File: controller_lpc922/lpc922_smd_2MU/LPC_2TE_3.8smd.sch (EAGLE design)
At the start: 46 parts, among them IC1 MC34063AD, Q1 BC856, Q2 BC847C, Q3 BCP52

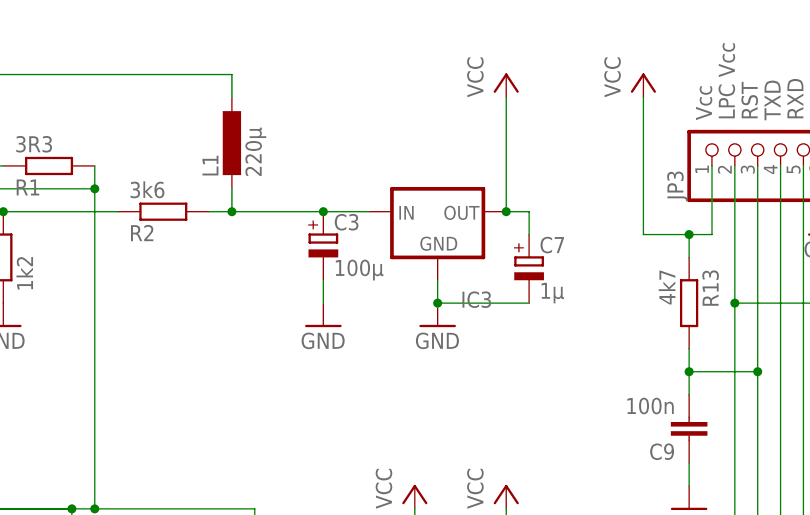
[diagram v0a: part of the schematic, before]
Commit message: Type of LDO added (VALUE in Schematic and Board added).
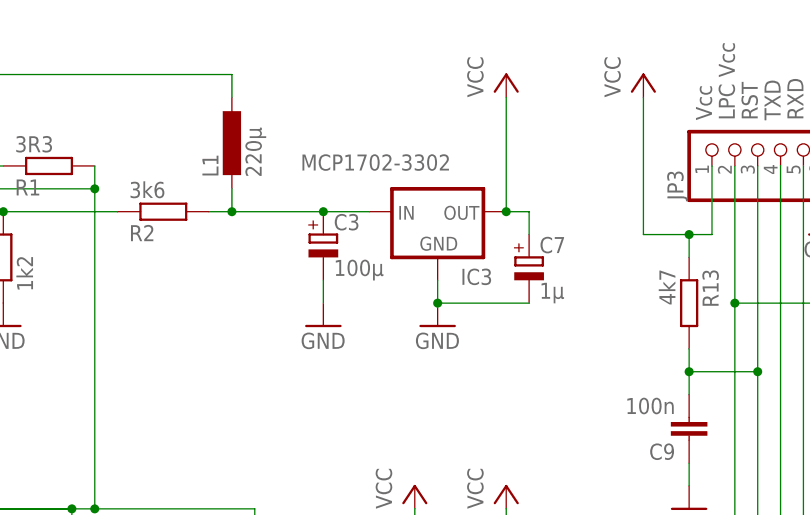
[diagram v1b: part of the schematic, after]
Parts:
- IC3: value (none) -> MCP1702-3302
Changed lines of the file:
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@@
 <part name="Q4" library="crystal" deviceset="ASF*" device="" technology="L1"/>
 <part name="GND3" library="supply1" deviceset="GND" device=""/>
-<part name="IC3" library="v-reg" deviceset="79LXX" device=""/>
+<part name="IC3" library="v-reg" deviceset="79LXX" device="" value="MCP1702-3302"/>
 <part name="C7" library="rcl" deviceset="CPOL-EU" device="E2-5" value="1µ"/>
 <part name="Q2" library="transistor-npn" deviceset="BC847*" device="SMD" technology="C" value="BC847C"/>
@@
 </instance>
 <instance part="IC3" gate="A" x="134.62" y="152.4" smashed="yes" rot="MR180">
-<attribute name="NAME" x="137.16" y="143.51" size="1.778" layer="95" rot="MR180"/>
-<attribute name="VALUE" x="137.16" y="146.05" size="1.778" layer="96" rot="MR180"/>
+<attribute name="NAME" x="137.16" y="146.05" size="1.778" layer="95" rot="MR180"/>
+<attribute name="VALUE" x="119.38" y="158.75" size="1.778" layer="96" rot="MR180"/>
 </instance>
 <instance part="C7" gate="G$1" x="144.78" y="147.32" smashed="yes">

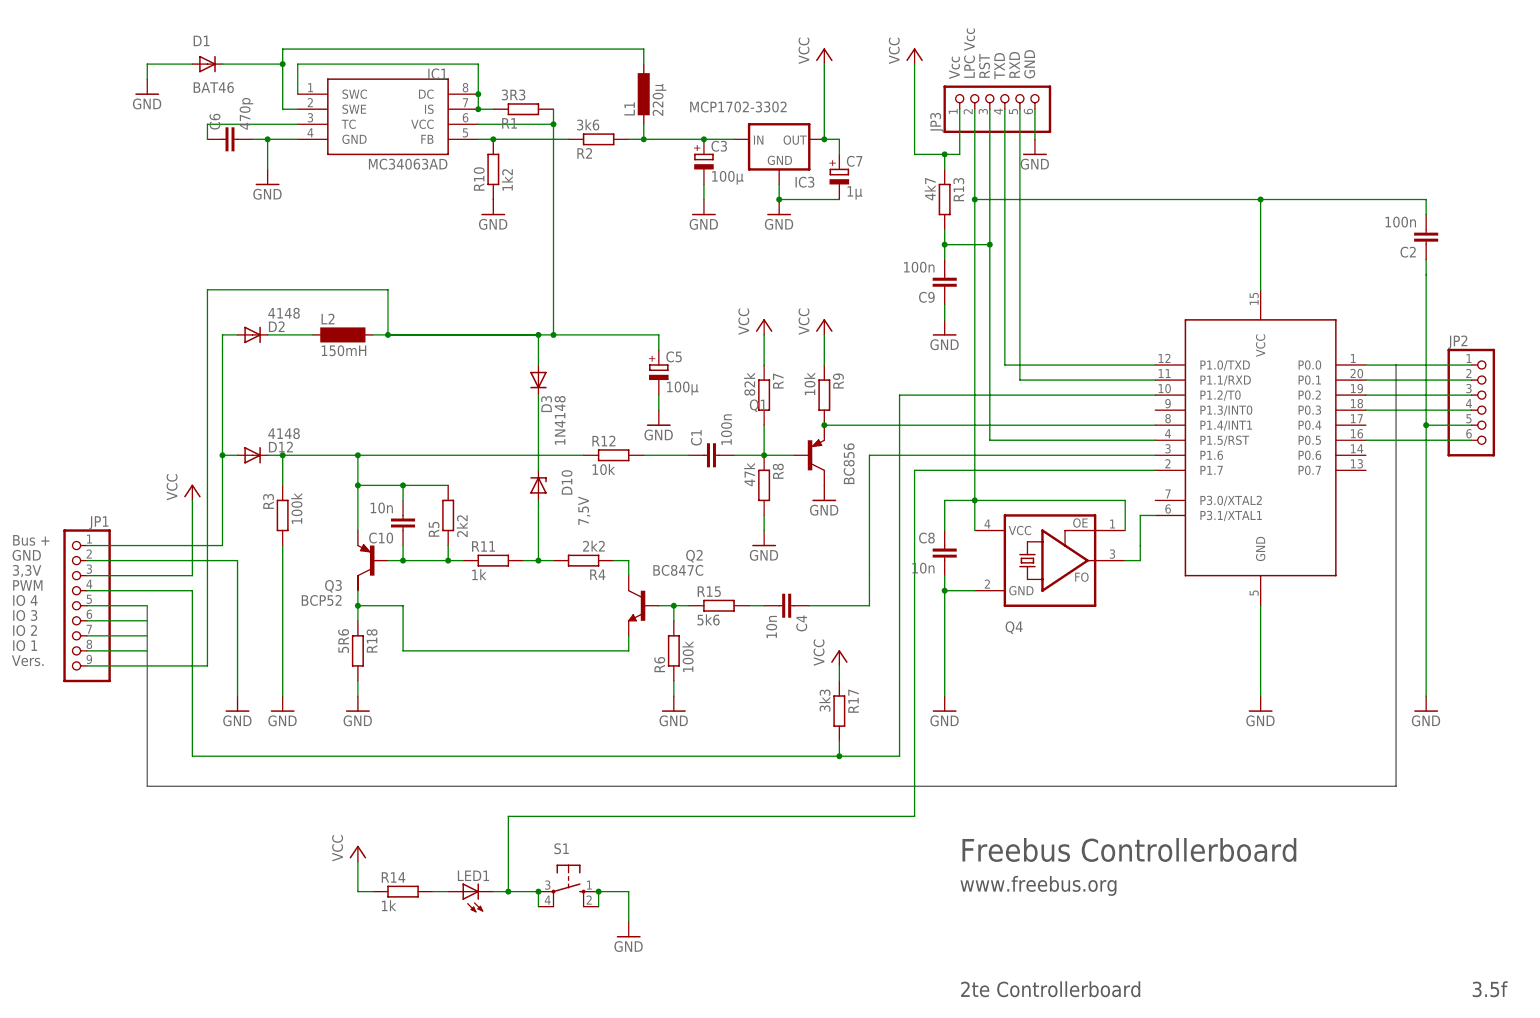
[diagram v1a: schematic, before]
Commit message: 3D models added + some rework
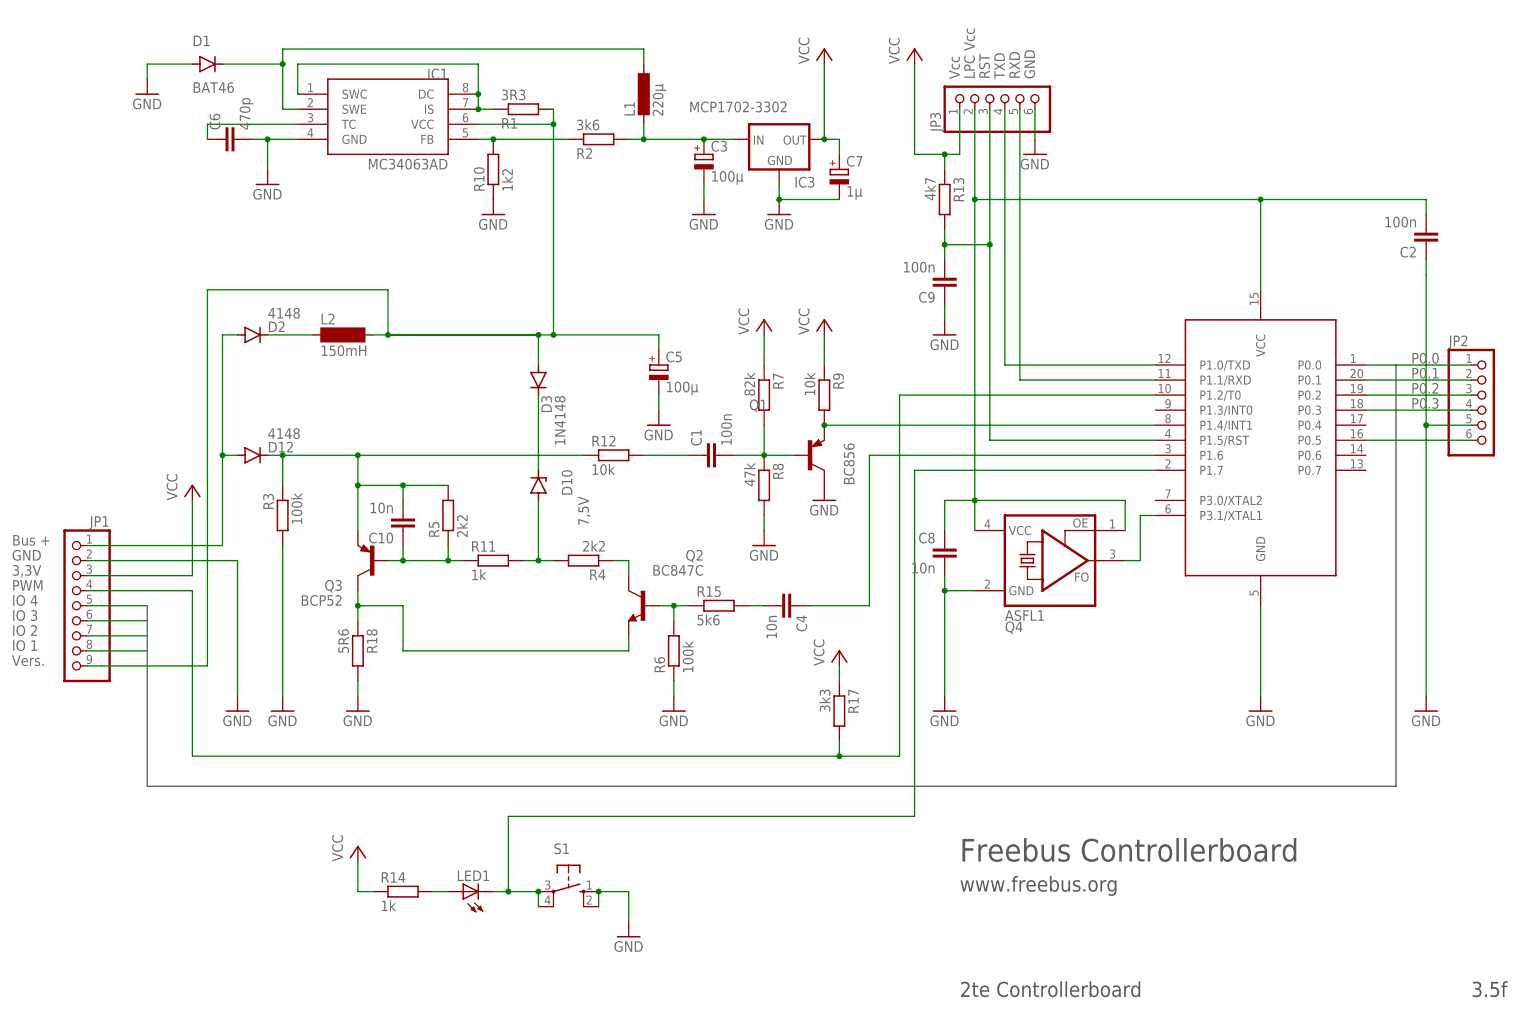
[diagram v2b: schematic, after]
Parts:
- 89LPC922: device micro-philips:89LPC922 -> MyIC-MCU:89LPC922
- JP1: device pinhead:PINHD-1X9 -> pinhead-1:PINHD-1X9_LONG_2.54
- Q4: value (none) -> ASFL1
